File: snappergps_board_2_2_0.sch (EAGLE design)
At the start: 66 parts, among them IC1 W25N512GVEIG_W25N512GVEIG, J1 DX07S016JA1R1500, J4 2988, J5 2988, Q1 TT8M1TRAMANDA, Q3 TT8M1TRAMANDA, Q4 TT8M1TRAMANDA, U1 EFM32HG310F64, U2 RF_CIRCUIT-SE4150L, U3 TVS_DIODE-PRTR5V0U2AX, U6 TPS61291DRVT, U7 MDMK2020T3R3MM

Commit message: Tweak schematic
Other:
- note removed: "SnapperGPS zebra logo"
- note removed: "Using Al's desgin as inspiration: https://github.com/arribada/horizon/blob/master/hardware/horizon_v4_1/"
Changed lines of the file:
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@@
 <part name="FRAME1" library="SparkFun-Aesthetics" deviceset="FRAME-A4L" device="">
 <attribute name="CNAME" value="RF front end"/>
-<attribute name="CREVISION" value="2.9"/>
+<attribute name="CREVISION" value="2.2.0"/>
 <attribute name="DESIGNER" value="A. Rogers, J. Beuchert"/>
-<attribute name="REV" value="2.4"/>
+<attribute name="REV" value="2.2.0"/>
 </part>
 <part name="FRAME2" library="SparkFun-Aesthetics" deviceset="FRAME-A4L" device="">
 <attribute name="CNAME" value="Flash, power, LEDs, and LFXTAL"/>
-<attribute name="CREVISION" value="2.9"/>
+<attribute name="CREVISION" value="2.2.0"/>
 <attribute name="DESIGNER" value="A. Rogers, J. Beuchert"/>
 </part>
 <part name="FRAME3" library="SparkFun-Aesthetics" deviceset="FRAME-A4L" device="">
 <attribute name="CNAME" value="USB and power"/>
-<attribute name="CREVISION" value="2.9"/>
+<attribute name="CREVISION" value="2.2.0"/>
 <attribute name="DESIGNER" value="A. Rogers, J. Beuchert"/>
 </part>
 <part name="FRAME4" library="SparkFun-Aesthetics" deviceset="FRAME-A4L" device="">
 <attribute name="CNAME" value="MCU IO connections"/>
-<attribute name="CREVISION" value="2.9"/>
+<attribute name="CREVISION" value="2.2.0"/>
 <attribute name="DESIGNER" value="A. Rogers"/>
 </part>
@@
 <sheet>
 <plain>
-<text x="-251.46" y="231.14" size="1.778" layer="91">Using Al's desgin as inspiration:
-https://github.com/arribada/horizon/blob/master/hardware/horizon_v4_1/</text>
-<text x="-251.46" y="226.06" size="1.778" layer="91">SnapperGPS zebra logo</text>
 </plain>
 <instances>
@@
 </drawing>
 <compatibility>
-<note version="6.3" minversion="6.2.2" severity="warning">
-Since Version 6.2.2 text objects can contain more than one line,
-which will not be processed correctly with this version.
-</note>
 <note version="8.2" severity="warning">
 Since Version 8.2, EAGLE supports online libraries. The ids

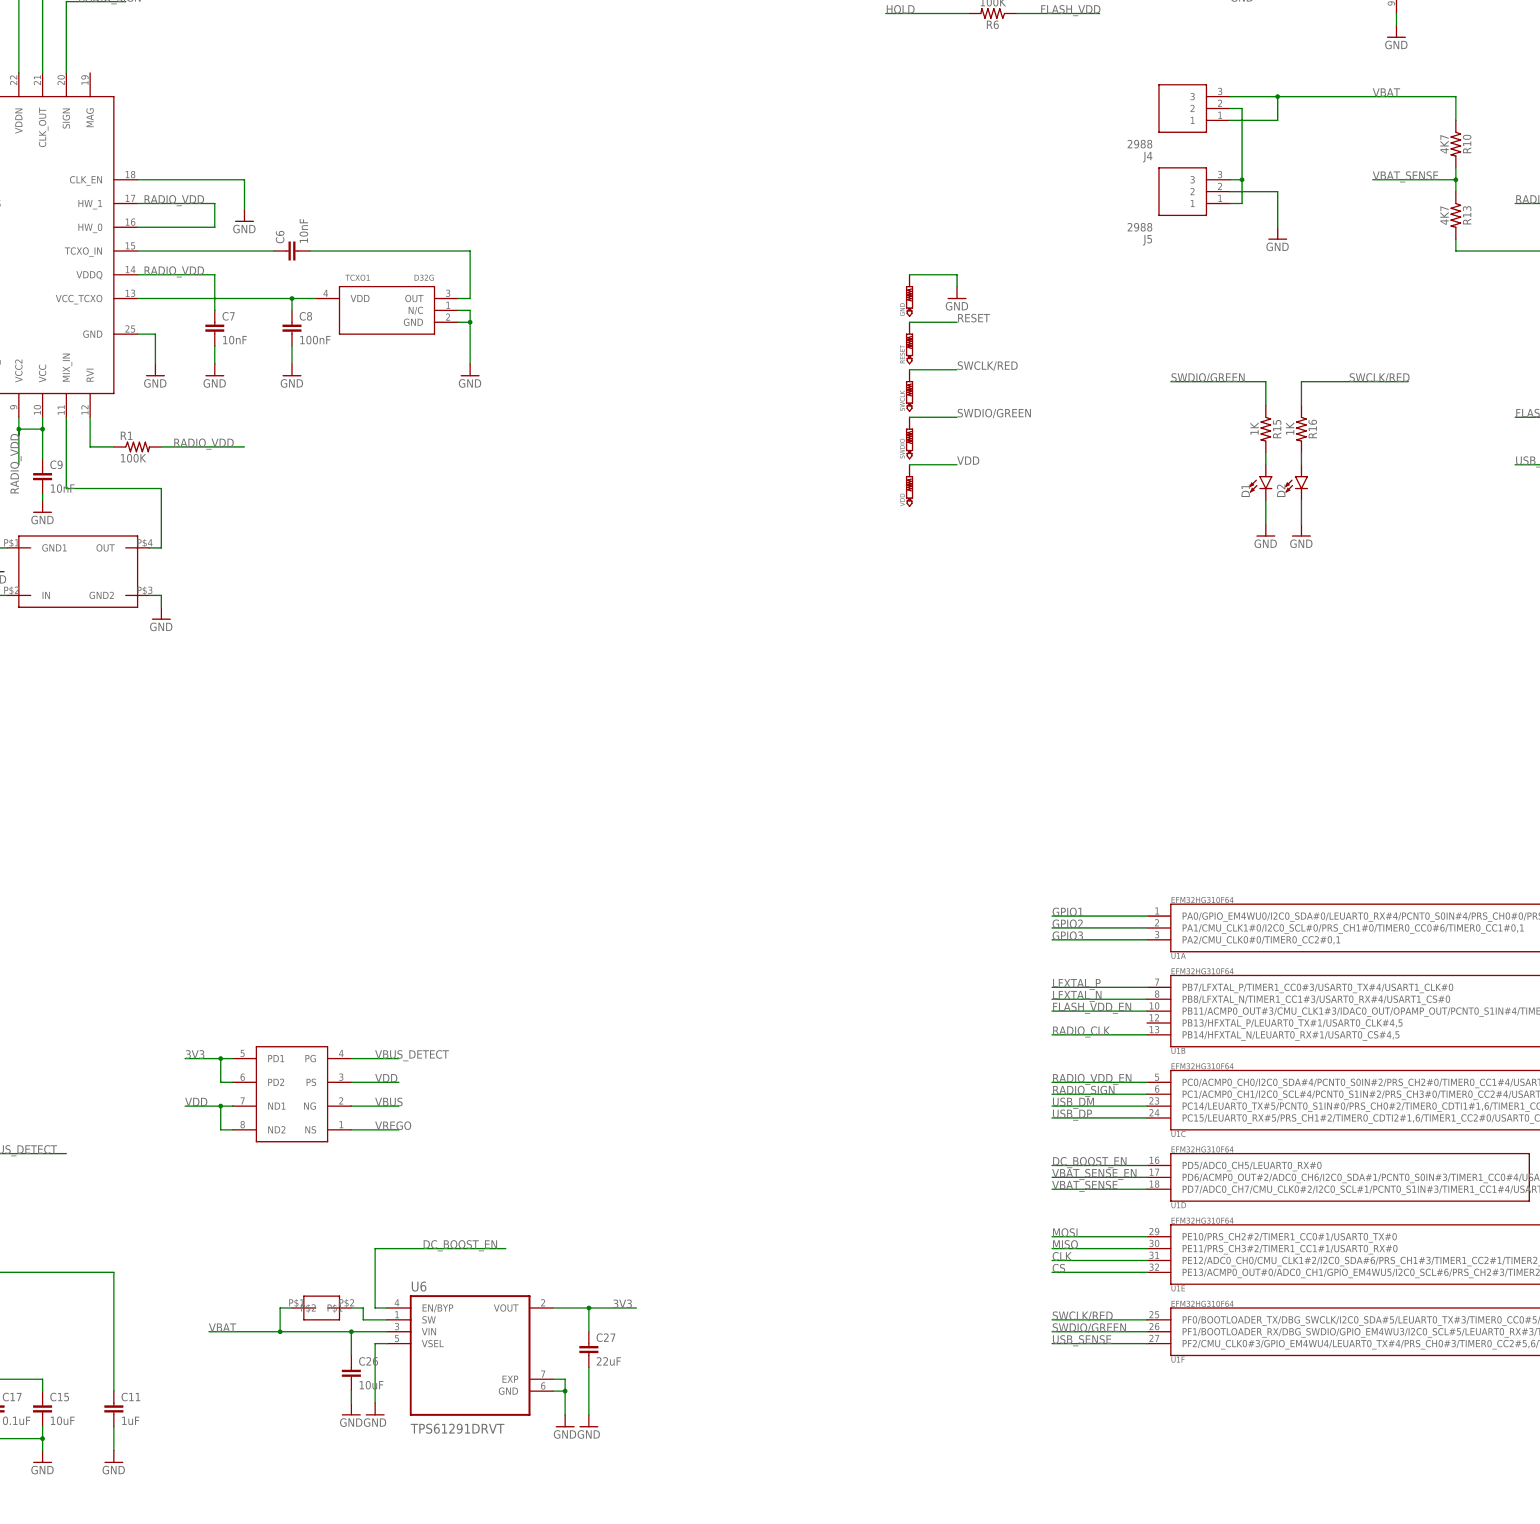
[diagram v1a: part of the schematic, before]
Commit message: Replace coin cells with lipo, add lipo charger
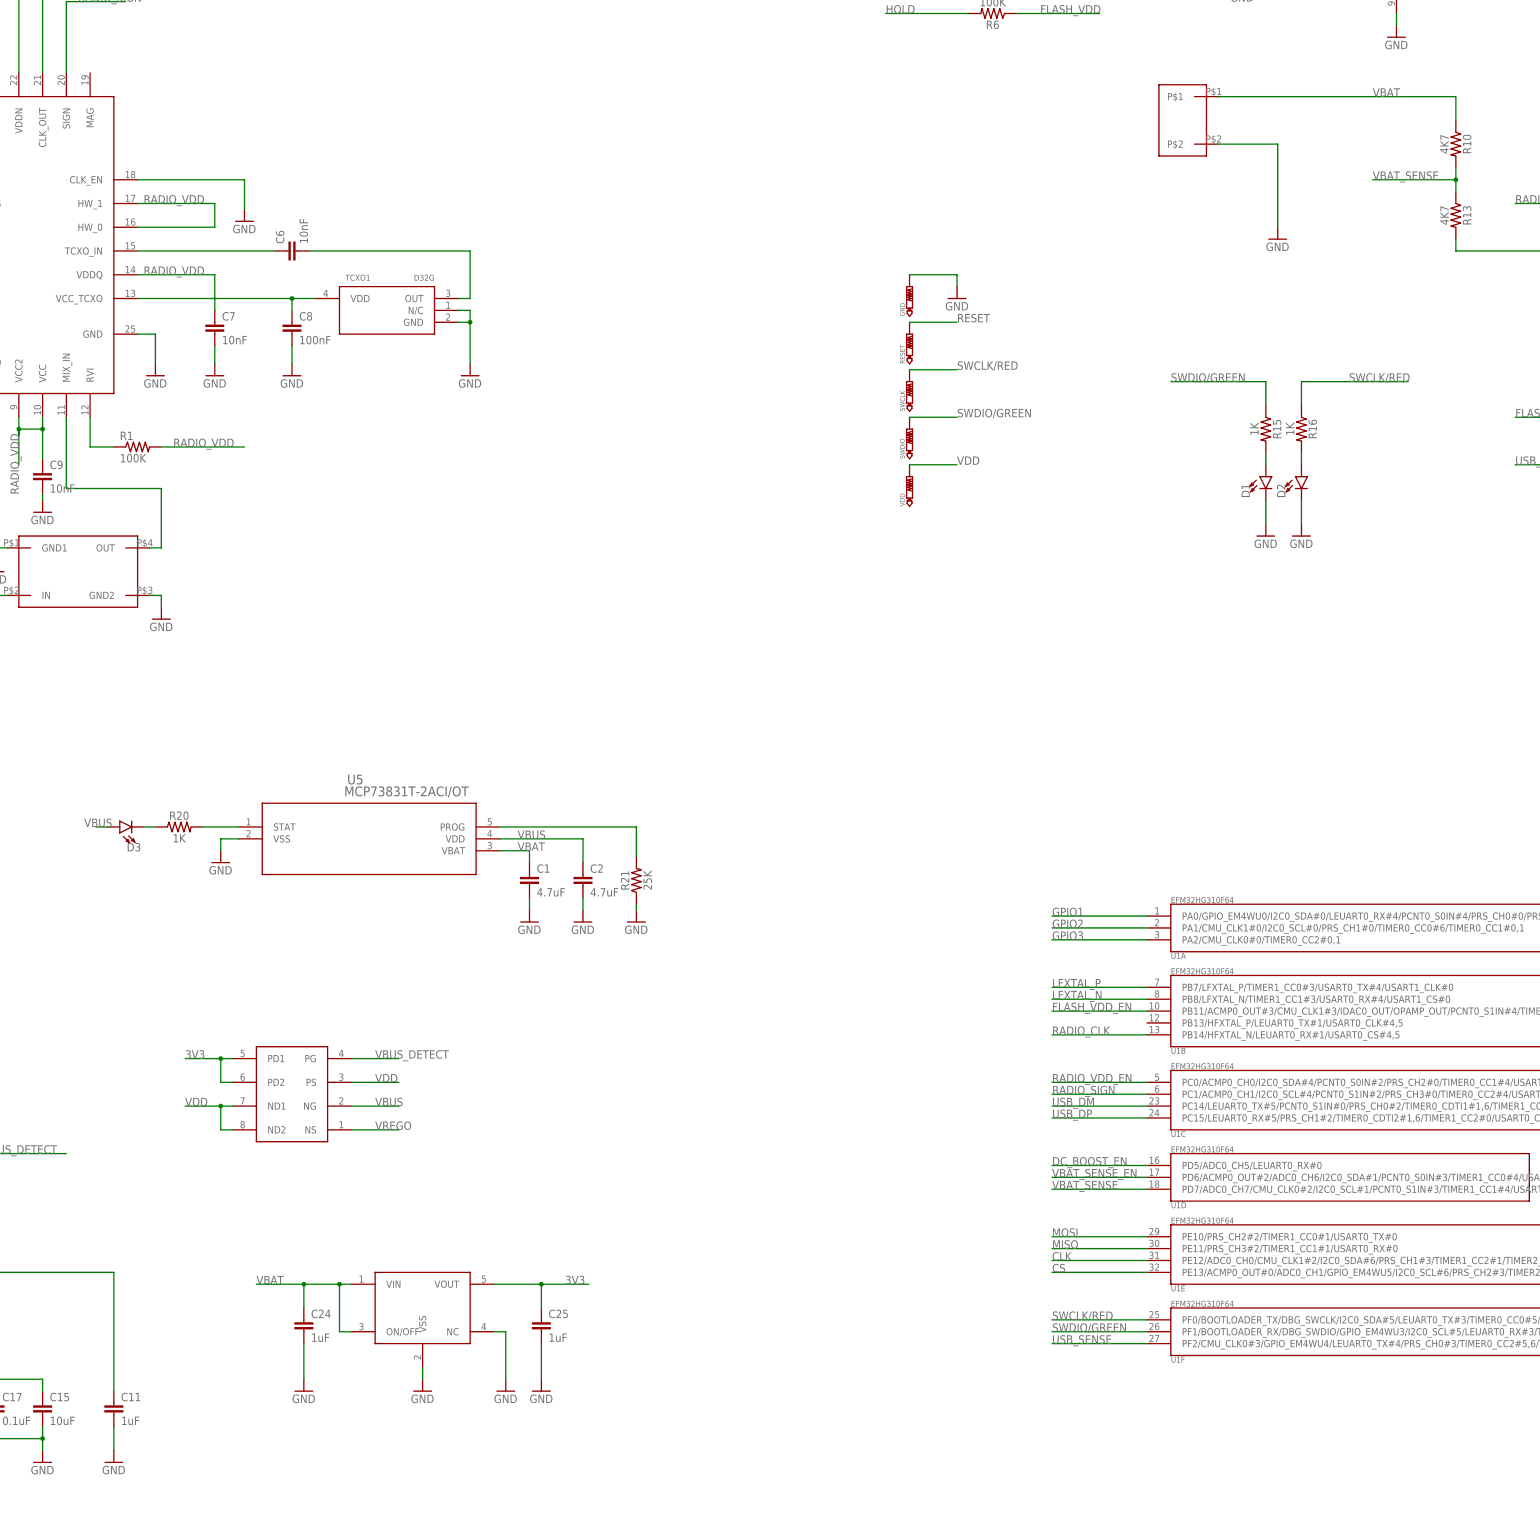
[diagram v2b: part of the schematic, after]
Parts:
- removed C26: 10uF, rcl:C-EUC0603K
- removed C27: 22uF, rcl:C-EUC0603K
- removed J4, J5: 2988, 2988:2988
- removed U6: TPS61291DRVT, TPS61291DRVT:TPS61291DRVT
- removed U7: MDMK2020T3R3MM, alex:MDMK2020T3R3MM
- added C1, C2: 4.7uF, bird_variant_2:CAPACITOR_0603
- added C24, C25: 1uF, bird_variant_2:CAPACITOR_0603
- added D3: (no value), bird_variant_2:LED0603
- added R20: 1K, bird_variant_2:RESISTOR_0402
- added R21: 25K, bird_variant_2:RESISTOR_0402
- added U$3: INDUCTION_BOARD_CONN2, inductive_sensor_daughterboard:INDUCTION_BOARD_CONN2
- added U4: S-1318D33-M5T1U4, SOT95P280X145-5N-volt:S-1318D33-M5T1U4
- added U5: MCP73831T-2ACI/OT, mcp73831T-2ACI:MCP73831T-2ACI/OT
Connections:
- removed net N$20: J4.2, J5.1, J5.3
- new net N$15: R20.2, U5.STAT
- new net N$21: R21.2, U5.PROG
- net 3V3: now also C25.1, U4.VOUT; no longer C27.1, U6.VOUT
- net DC_BOOST_EN: no longer U6.EN/BYP
- net GND: now also C1.2, C2.2, C24.2, C25.2, R21.1, U$3.P$2, U4.NC, U4.VSS, U5.VSS; no longer C26.2, C27.2, J5.2, U6.EXP, U6.GND, U6.VSEL
- net N$7: now also D3.C, R20.1; no longer U6.SW, U7.P$2
- net VBAT: now also C1.1, C24.1, U$3.P$1, U4.ON/OFF, U4.VIN, U5.VBAT; no longer C26.1, J4.1, J4.3, U6.VIN, U7.P$1
- net VBUS: now also C2.1, D3.A, U5.VDD

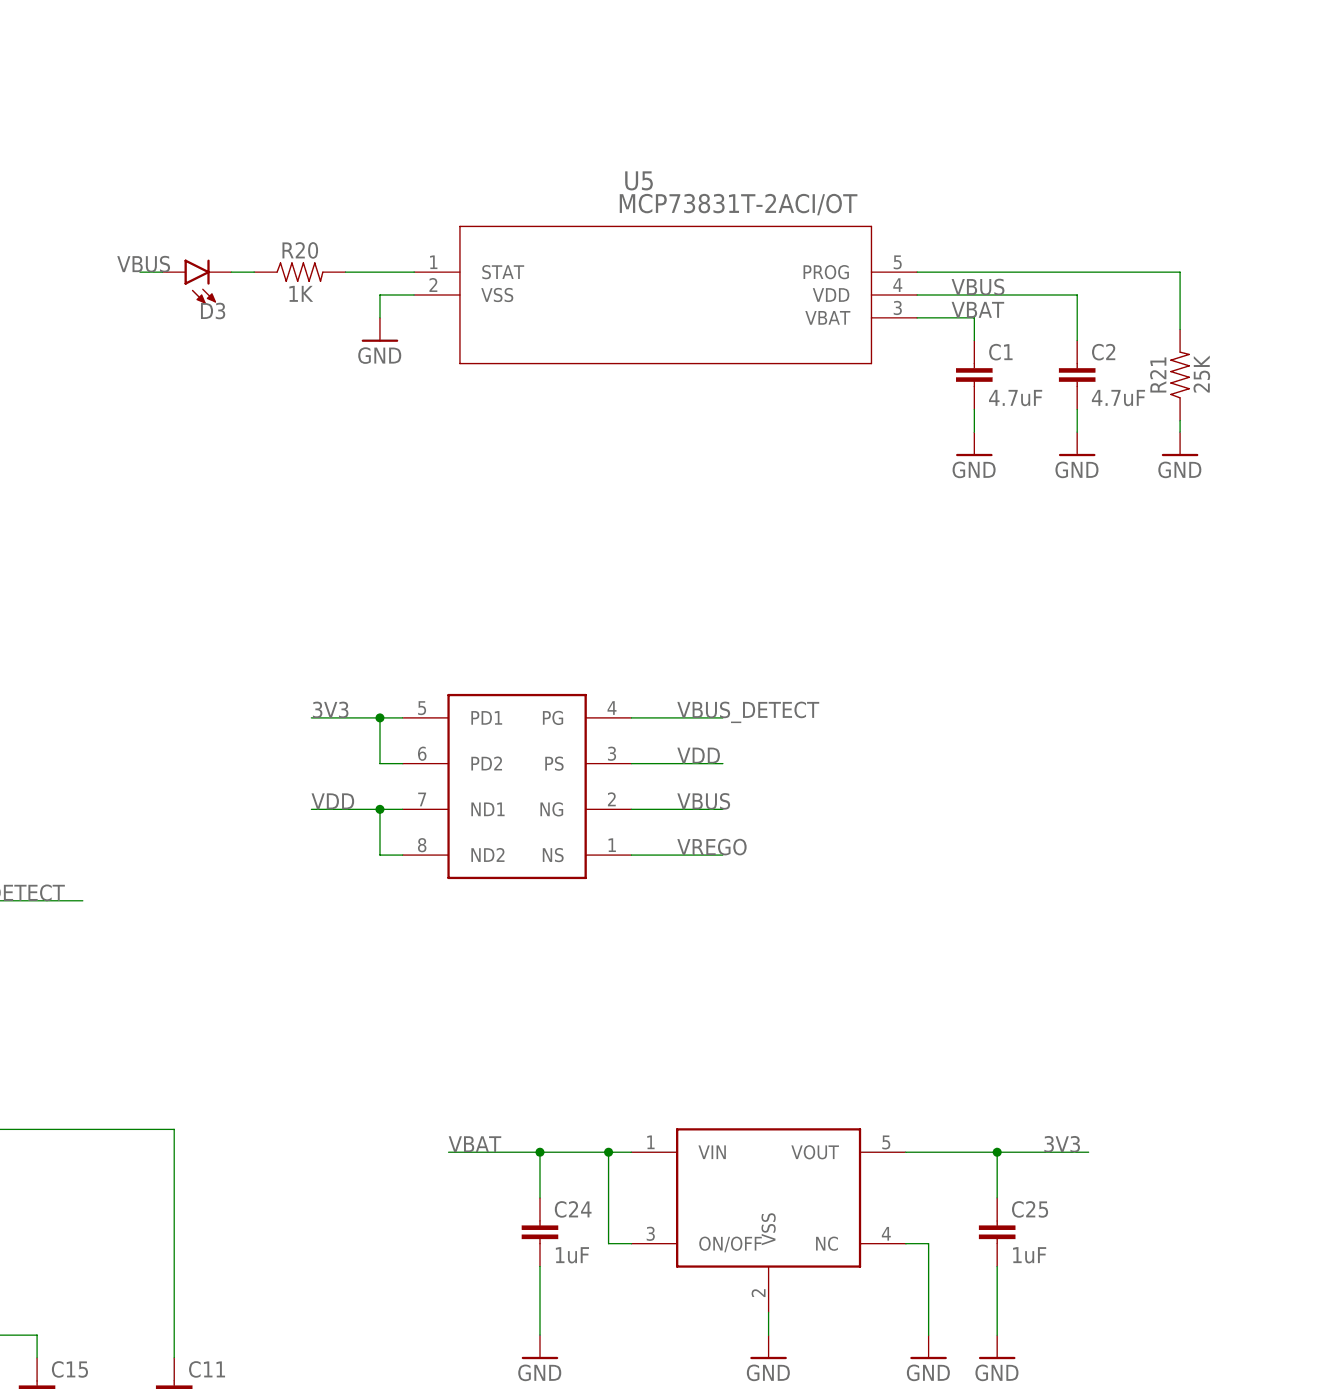
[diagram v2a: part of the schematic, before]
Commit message: Add manufacturing files & tweak PCB
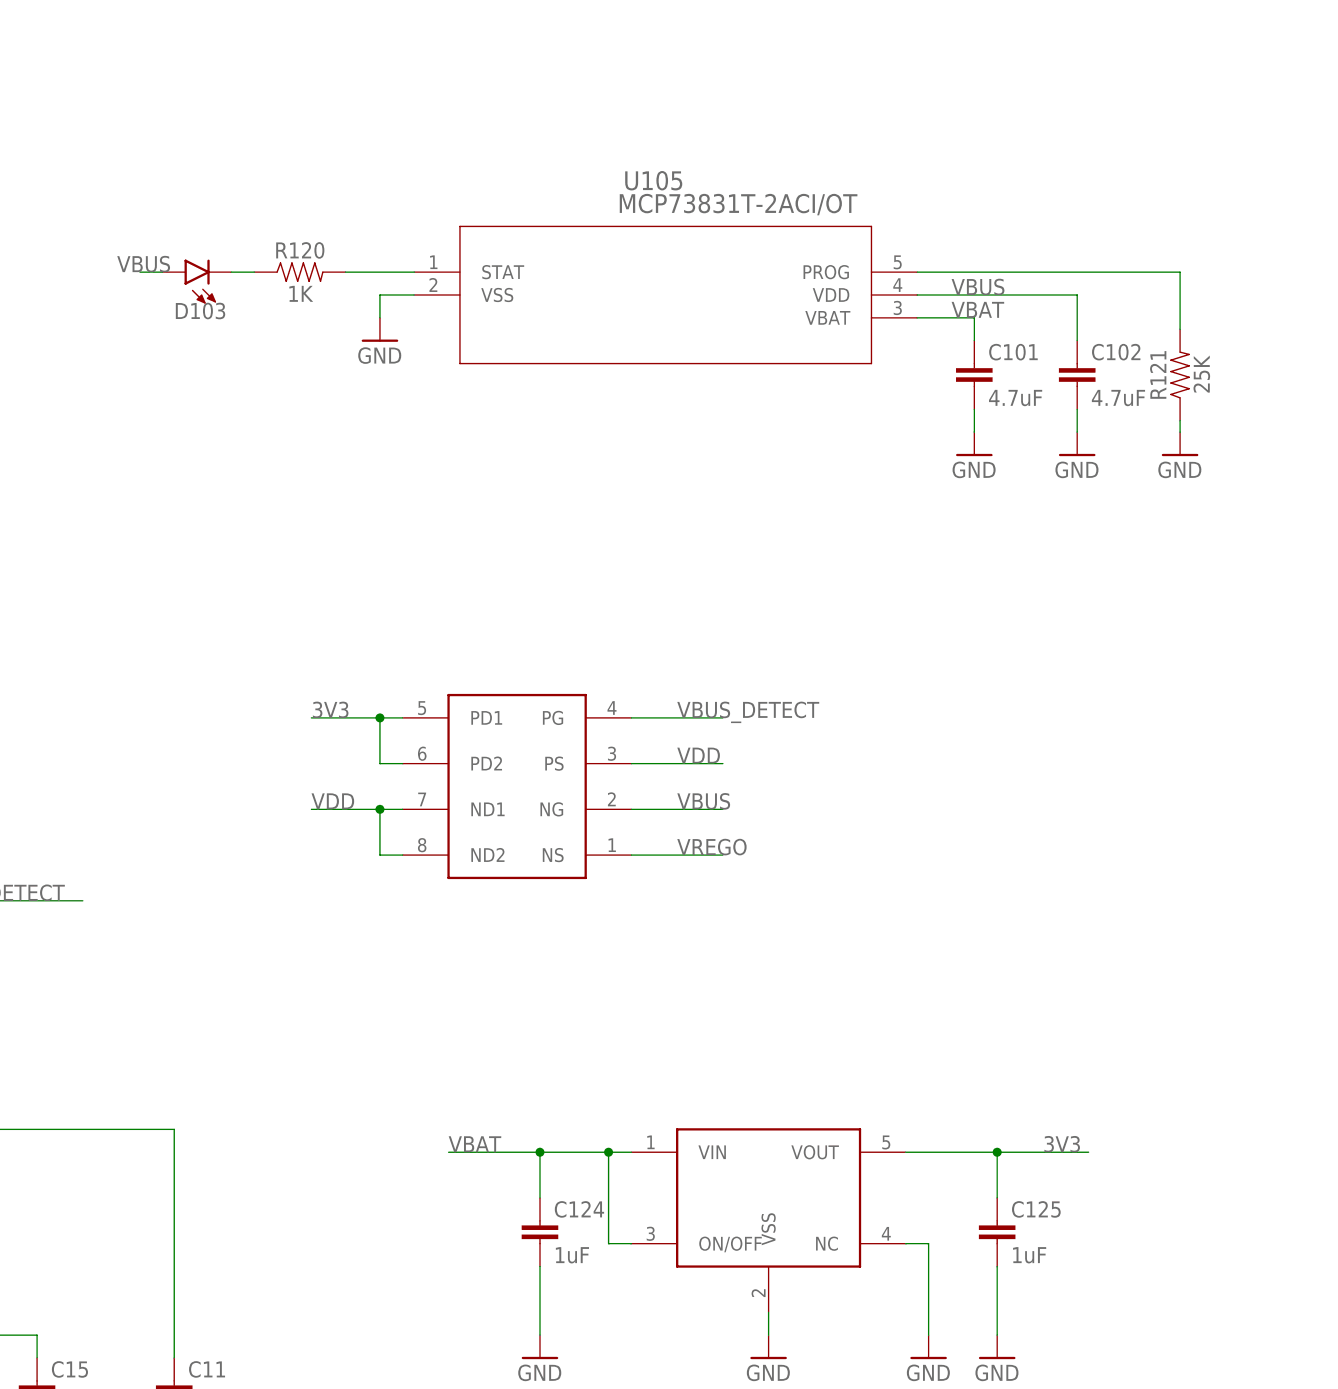
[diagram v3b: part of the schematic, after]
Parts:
- renumbered C1 to C101, C2 to C102, C24 to C124, C25 to C125, D3 to D103, R20 to R120, R21 to R121, U4 to U104, U5 to U105
